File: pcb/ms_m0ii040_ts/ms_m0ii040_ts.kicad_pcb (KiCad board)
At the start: 2 copper layers, 228.6 x 77.7 mm, 98 parts, among them J1 USB_C_Receptacle_USB2.0, J2 Conn_ARM_JTAG_SWD_10, SW1 ESC, SW10 O, SW11 P, SW13 CTRL, SW14 A, SW15 S, SW16 D, SW17 F, SW18 G, SW19 H, SW2 Q, SW20 J, SW21 K, SW22 L, SW23 ENT, SW25 SHIFT, SW26 Z, SW27 X, SW28 C, SW29 V, SW3 W, SW30 B, SW31 N, SW32 M, SW33 ,, SW34 ., SW35 SHIFT, SW38 WIN, SW39 ALT, SW4 E, SW40 BS, SW42 SPC, SW43 ALT, SW44 APP, SW5 R, SW6 T, SW7 Y, SW8 U, SW9 I, U1 STM32F072C8Tx, U2 TLV73333PDBV

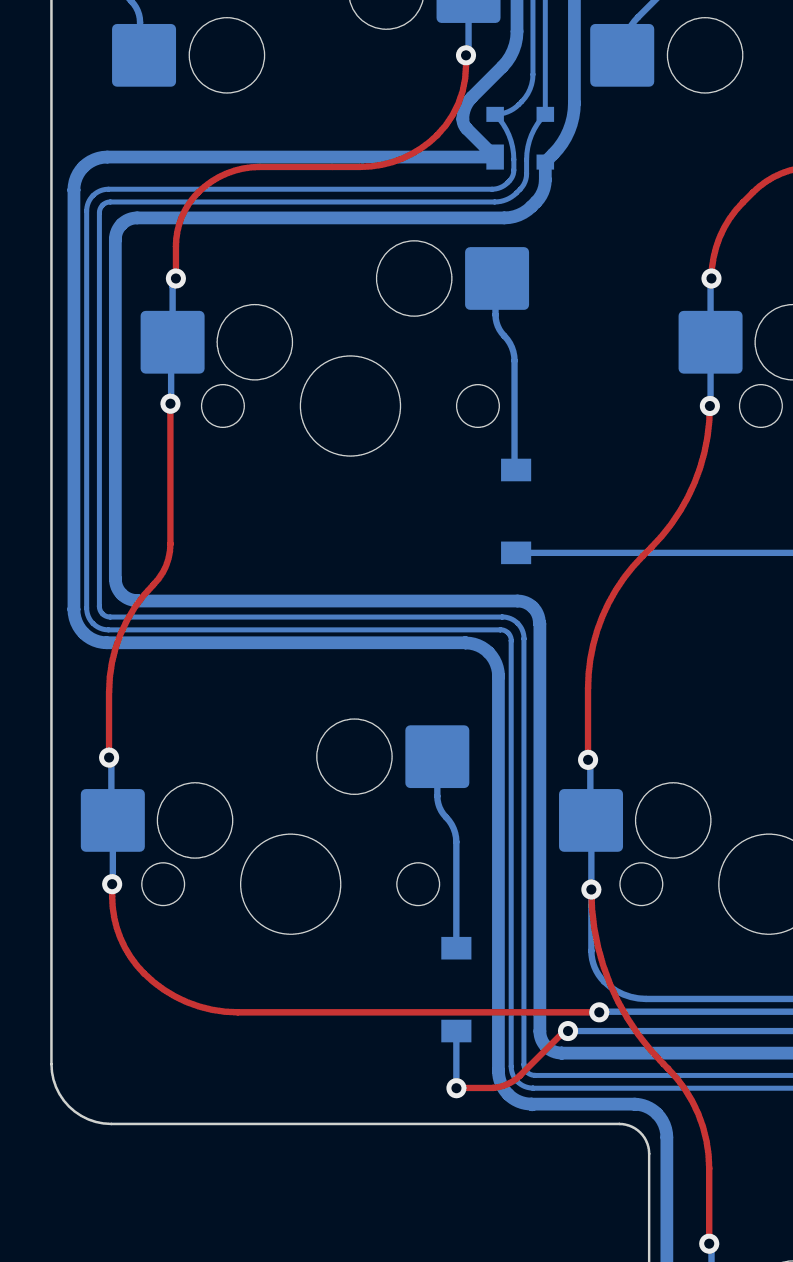
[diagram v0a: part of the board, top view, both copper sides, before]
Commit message: D- and GND slightly separated.
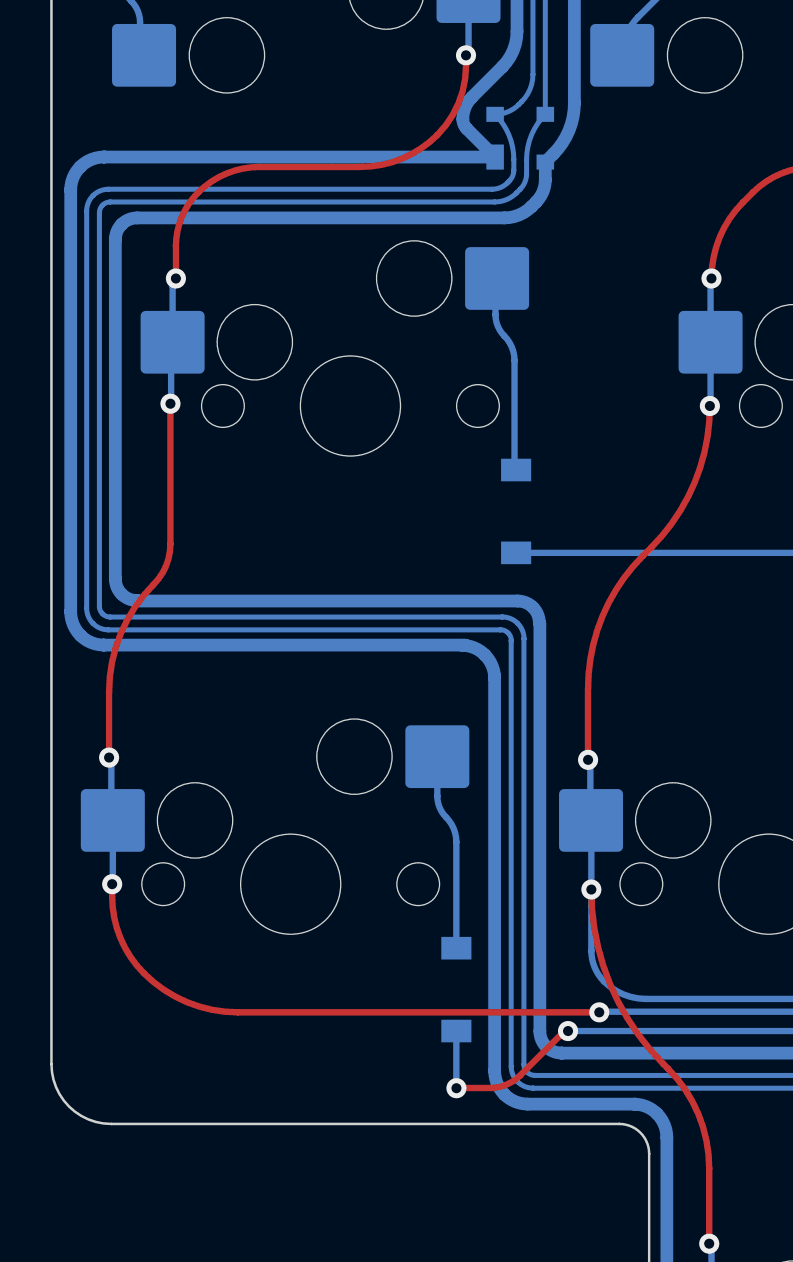
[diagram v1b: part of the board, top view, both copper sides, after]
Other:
- board text added: "M0ii040 Treadstone-staggered rev1.0.2 Copyright marksard 2023. Licensed under CERN-OHL-P v2"
- board text removed: "M0ii040 Treadstone-staggered rev1.0.1 Copyright marksard 2023. Licensed under CERN-OHL-P v2"
